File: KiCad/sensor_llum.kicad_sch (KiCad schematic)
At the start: 4 parts, among them U1 BH1750FVI-TR

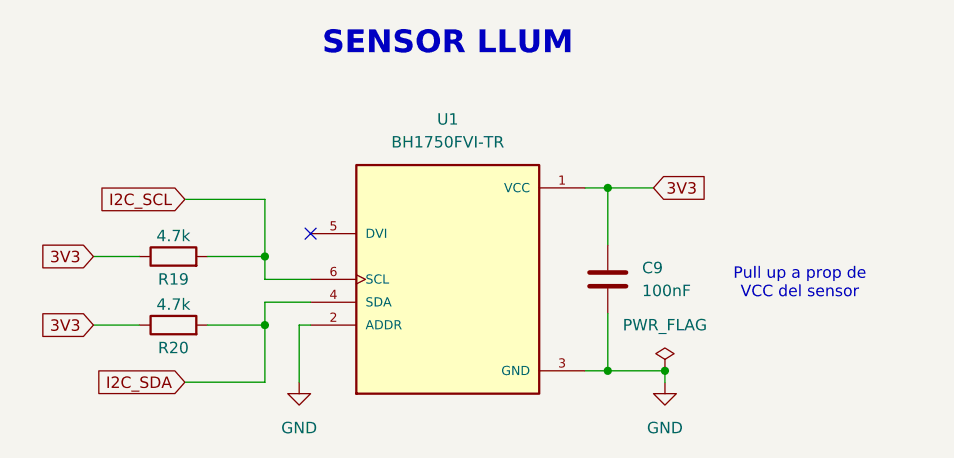
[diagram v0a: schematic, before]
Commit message: alguns errors de CADLAB i he canivat d'ordre els LEDs i els drivers a la PCB.
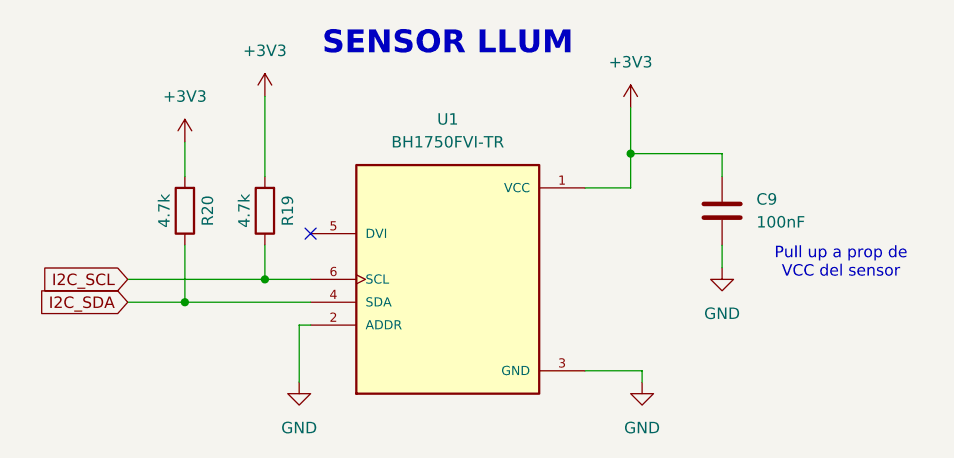
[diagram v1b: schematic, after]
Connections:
- net I2C_SCL: now also R19.1; no longer R19.2
- net I2C_SDA: now also R20.1; no longer R20.2
- net 3V3 renamed +3V3
- net +3V3: now also R19.2, R20.2; no longer R19.1, R20.1
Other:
- moved on the sheet: C9, R19, R20
